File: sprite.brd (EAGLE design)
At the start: 35 x 35 mm, 40 parts

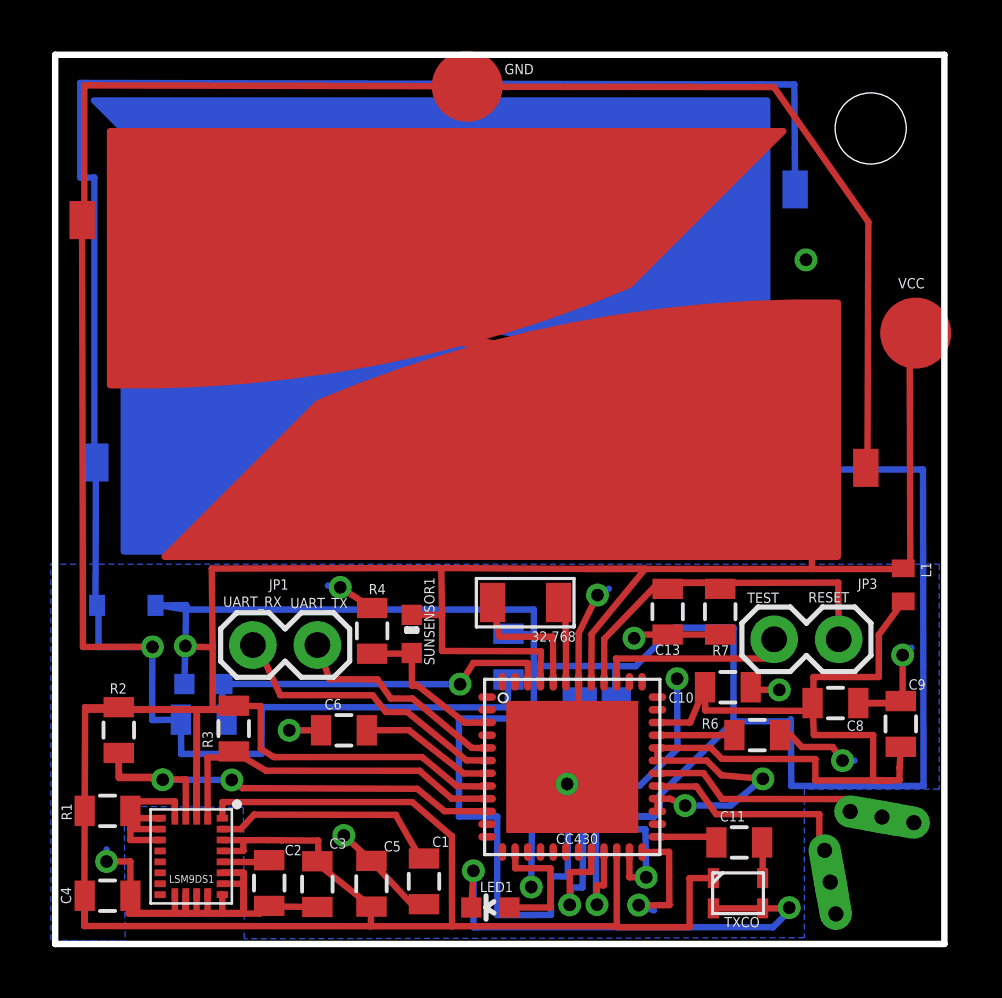
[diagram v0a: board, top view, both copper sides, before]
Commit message: fixed reset line, added current-limiting resistor and bypass cap
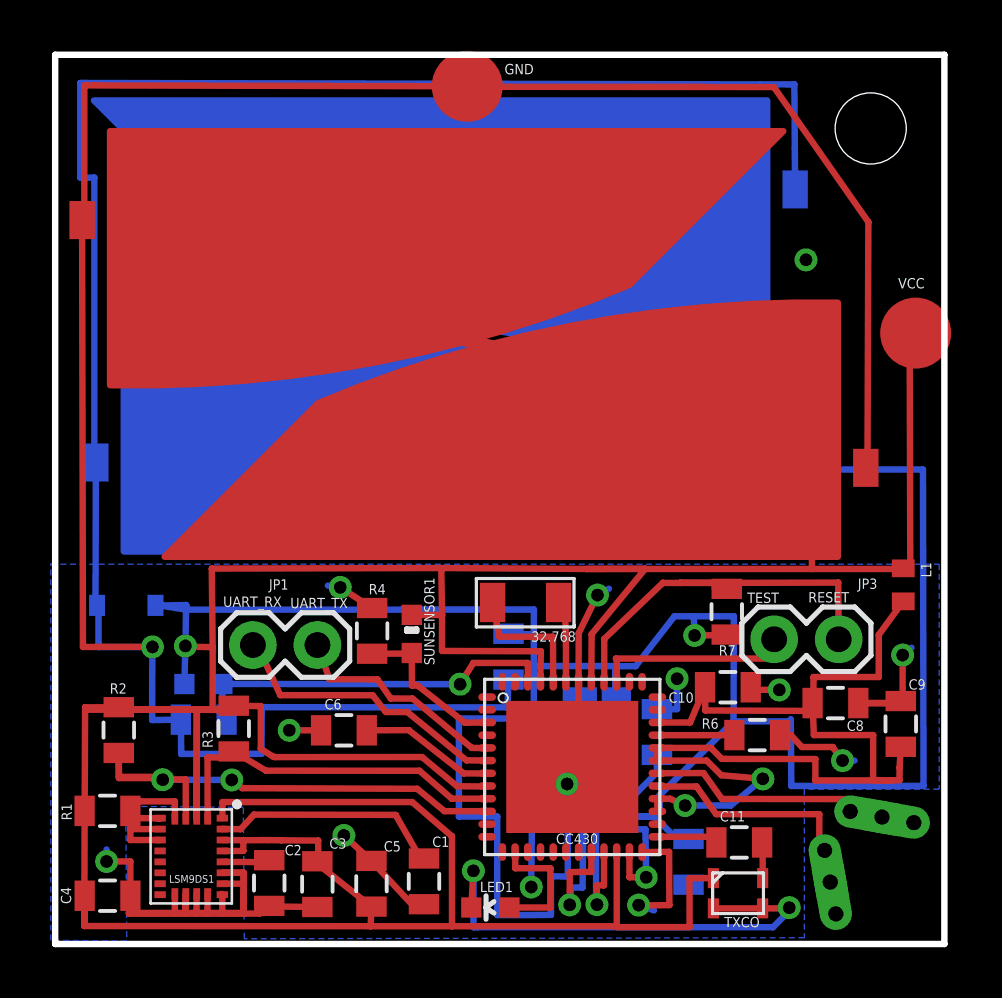
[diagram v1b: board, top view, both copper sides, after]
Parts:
- removed C13: 2.2nF, SparkFun:0805
- added C12: 10uF, SparkFun:0805
- added R8: 20, SparkFun:0805
- moved R7 0.26 mm to (26.4, 13.1)
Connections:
- new net LOADLINE: H-BRIDGE.OUT2, R8.2, RECTIFIER.PIN3
- net #RST/SBWTDIO: no longer C13.2
- net COIL1: now also R8.1; no longer H-BRIDGE.OUT2, RECTIFIER.PIN3
- net GND: now also C12.1; no longer C13.1, R7.1
- net VCC: now also C12.2, R7.1
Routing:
- net COIL1: track 1138.2 -> 1132.6 mm
- net LOADLINE: track 0.00 -> 4.77 mm
- net VCC: track 368.7 -> 373.2 mm, vias 1 -> 2
- net GND: track 230.3 -> 226.6 mm, vias 13 -> 12
- net #RST/SBWTDIO: track 16.9 -> 16.1 mm
